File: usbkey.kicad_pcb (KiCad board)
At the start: 2 copper layers, 12 x 11 mm, 15 parts, among them P1 USART0, P2 DEBUG, P3 USB_B, U1 EFM32HG309

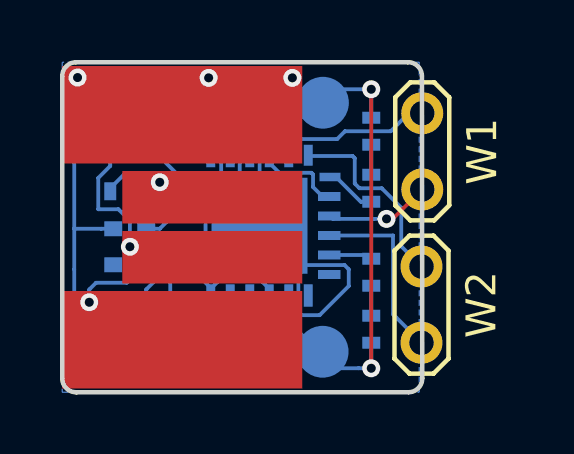
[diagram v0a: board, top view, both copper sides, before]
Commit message: Cleaning up the silk screen.
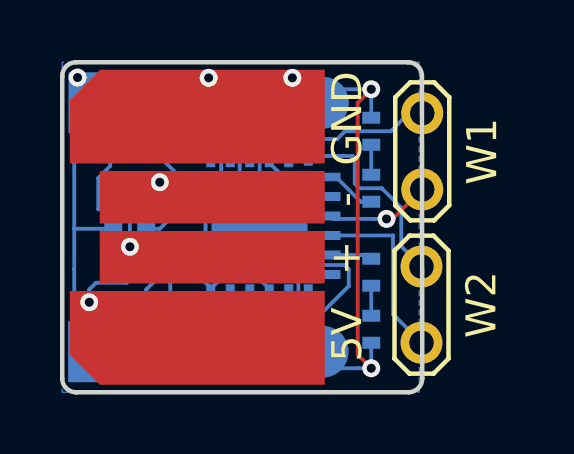
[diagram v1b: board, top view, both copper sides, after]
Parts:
- P1: footprint Pin_Headers:Pin_Header_Angled_1x04 -> debug-points
- P2: footprint Pin_Headers:Pin_Header_Angled_1x04 -> usb-pcb:debug-points
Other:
- board text added: "C"
- board text added: "D"
- board text added: "R"
- board text added: "T"
- board text removed: "Front - Debug Pads Bottom - IC"

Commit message: Temp commit.
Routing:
- net GND: track 39.4 -> 38.0 mm
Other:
- rule pad_to_mask_clearance: 0.2 -> 0.1

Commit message: PCB improvements.
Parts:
- added REF**: Measurement_Point_Round-TH_Small, Measurement_Points:Measurement_Point_Round-TH_Small, F.Cu at (0.00, 0.00)
- W1, W2: footprint Measurement_Points:Test_Point_2Pads -> usb-pcb:minimal-points; moved to B.Cu
- moved W1 1.39 mm to (28.5, 21.0)
- moved W2 1.05 mm to (28.5, 25.8)
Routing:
- net /USB_5V: track 4.59 -> 9.92 mm
- net GND: track 38.0 -> 41.2 mm
- net /CAP1B: track 6.55 -> 7.63 mm, vias 0 -> 1
- net /CAP0B: track 5.17 -> 6.10 mm, vias 0 -> 1
- net /CAP0A: track 3.56 -> 3.97 mm, vias 1 -> 2
- net /CAP1A: track 6.09 -> 5.86 mm, vias 0 -> 1
- added copper zone on B.Cu, net /CAP0A
- added copper zone on F.Cu, net /CAP0A
- added copper zone on B.Cu, net /CAP0B
- added copper zone on F.Cu, net /CAP0B
- added copper zone on B.Cu, net /CAP1A
- added copper zone on F.Cu, net /CAP1A
- added copper zone on B.Cu, net /CAP1B
- added copper zone on F.Cu, net /CAP1B
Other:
- board size 12 x 11 mm -> 13 x 11 mm
- board text added: "microusbkey"
